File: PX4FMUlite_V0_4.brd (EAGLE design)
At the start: 48.6 x 34.9 mm, 126 parts, among them J2 DF13-4P-1.25V, J201 DF13C-6P-1.25V, J202 DF13C-6P-1.25V, J203 DF13C-6P-1.25V, J3 DF13C-4P-1.25V, J302 DF13C-4P-1.25V, J401 DF13C-4P-1.25V, J403 DF13C-7P-1.25V, J405 DF13C-4P-1.25V, J802 DF13C-3P-1.25V, M3_MOUNT1101 MOUNT-HOLE3.1MM, M3_MOUNT1102 MOUNT-HOLE3.1MM, M3_MOUNT1103 MOUNT-HOLE3.1MM, M3_MOUNT1104 MOUNT-HOLE3.1MM, U101 STM32F4X7VX, U2 MAX3051, U401 MAX3051, X101 3.2x2.5 mm / 24 MHz / 15 ppm

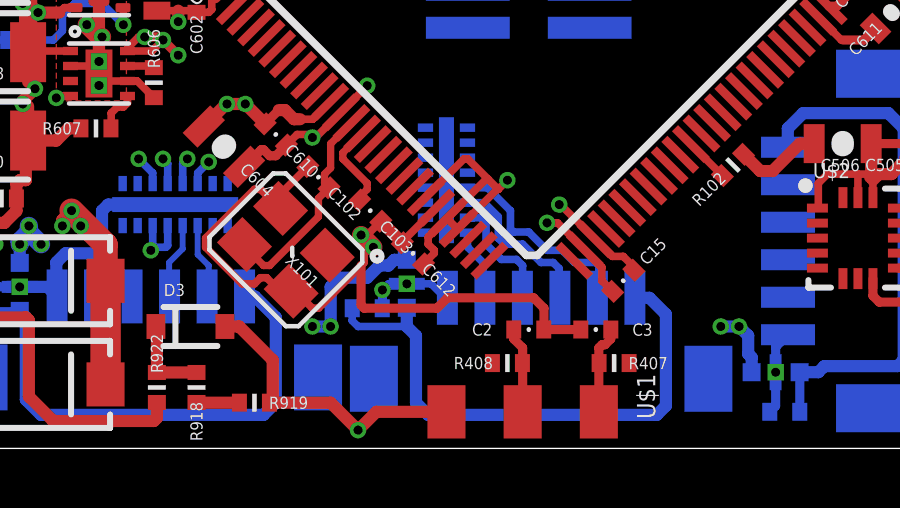
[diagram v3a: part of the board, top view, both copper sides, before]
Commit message: Tweaked power fills to prevent them being isolated after autoroute
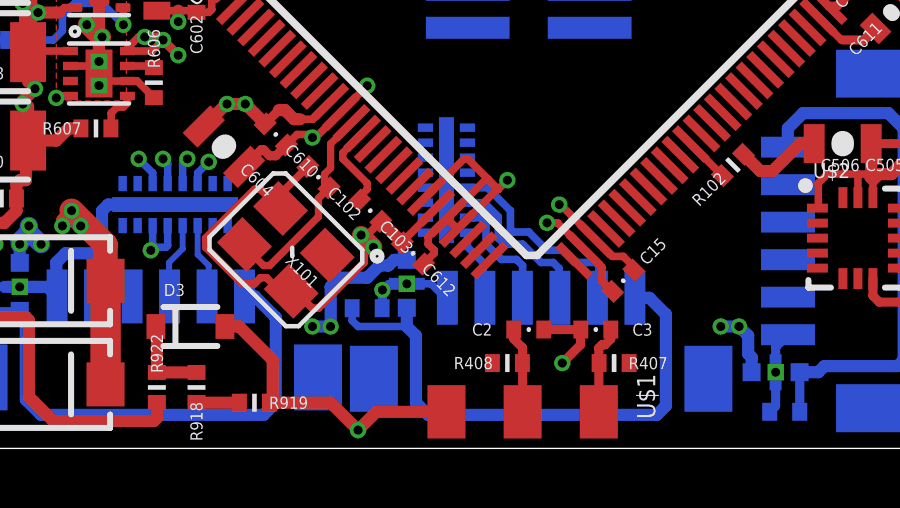
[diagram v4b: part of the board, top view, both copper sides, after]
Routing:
- net GND: track 206.8 -> 199.7 mm, vias 39 -> 40
- net VDD_IN: track 71.6 -> 70.6 mm
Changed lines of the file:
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@@
 <layer number="1" name="Top" color="4" fill="1" visible="yes" active="yes"/>
 <layer number="2" name="Ground" color="2" fill="10" visible="no" active="yes"/>
-<layer number="3" name="Horizontal" color="13" fill="15" visible="no" active="yes"/>
+<layer number="3" name="Horizontal" color="13" fill="15" visible="yes" active="yes"/>
 <layer number="4" name="Route4" color="1" fill="4" visible="no" active="no"/>
 <layer number="5" name="Route5" color="4" fill="4" visible="no" active="no"/>
@@
 <layer number="12" name="Route12" color="1" fill="5" visible="no" active="no"/>
 <layer number="13" name="Route13" color="4" fill="5" visible="no" active="no"/>
-<layer number="14" name="Vertical" color="14" fill="15" visible="no" active="yes"/>
-<layer number="15" name="Power" color="11" fill="15" visible="no" active="yes"/>
+<layer number="14" name="Vertical" color="14" fill="15" visible="yes" active="yes"/>
+<layer number="15" name="Power" color="11" fill="15" visible="yes" active="yes"/>
 <layer number="16" name="Bottom" color="1" fill="1" visible="yes" active="yes"/>
 <layer number="17" name="Pads" color="2" fill="1" visible="yes" active="yes"/>
@@
 <contactref element="U101" pad="6"/>
 <contactref element="R608" pad="P$1"/>
-<wire x1="30.273071875" y1="15.71561875" x2="27.2288" y2="18.1944" width="0" layer="19" extent="1-16"/>
+<wire x1="27.2288" y1="18.1944" x2="30.273071875" y2="15.71561875" width="0" layer="19" extent="1-16"/>
 </signal>
 <signal name="N$11">
@@
 <wire x1="22.7584" y1="10.16" x2="23.368" y2="10.16" width="0.8128" layer="15"/>
 <wire x1="46.6344" y1="30.6832" x2="45.4152" y2="30.6832" width="0.6096" layer="15"/>
-<wire x1="32.4104" y1="29.8704" x2="30.8864" y2="28.3464" width="1.016" layer="15"/>
-<wire x1="30.8864" y1="28.3464" x2="28.6512" y2="28.3464" width="1.016" layer="15"/>
-<wire x1="28.6512" y1="28.3464" x2="27.3304" y2="27.0256" width="1.016" layer="15"/>
+<wire x1="34.1376" y1="33.8328" x2="27.3304" y2="27.0256" width="1.016" layer="15"/>
 <wire x1="27.3304" y1="27.0256" x2="25.6032" y2="27.0256" width="1.016" layer="15"/>
 <wire x1="25.6032" y1="27.0256" x2="24.2824" y2="25.7048" width="1.016" layer="15"/>
 <wire x1="24.2824" y1="25.7048" x2="24.2824" y2="24.892" width="1.016" layer="15"/>
-<wire x1="32.4104" y1="29.8704" x2="33.528" y2="30.988" width="0.8128" layer="15"/>
-<wire x1="33.528" y1="30.988" x2="33.528" y2="32.7152" width="0.8128" layer="15"/>
-<wire x1="33.528" y1="32.7152" x2="34.6456" y2="33.8328" width="0.8128" layer="15"/>
-<wire x1="40.132" y1="33.8328" x2="34.6456" y2="33.8328" width="0.8128" layer="15"/>
+<wire x1="40.132" y1="33.8328" x2="34.1376" y2="33.8328" width="0.8128" layer="15"/>
 <wire x1="40.132" y1="33.8328" x2="40.132" y2="33.7312" width="0.8128" layer="15"/>
 <wire x1="40.132" y1="33.7312" x2="42.164" y2="31.6992" width="0.8128" layer="15"/>
@@
 <wire x1="33.373553125" y1="10.31444375" x2="32.8168" y2="9.757690625" width="0.254" layer="1"/>
 <wire x1="32.8168" y1="9.757690625" x2="32.8168" y2="8.9408" width="0.254" layer="1"/>
-<wire x1="32.8168" y1="8.9408" x2="32.7152" y2="8.8392" width="0.254" layer="1"/>
-<wire x1="32.7152" y1="8.8392" x2="31.2928" y2="7.4168" width="0.254" layer="1"/>
+<wire x1="32.8168" y1="8.9408" x2="31.2928" y2="7.4168" width="0.254" layer="1"/>
 <wire x1="31.2928" y1="7.4168" x2="31.0896" y2="7.4168" width="0.254" layer="1"/>
 <wire x1="31.0896" y1="7.4168" x2="30.522059375" y2="7.984340625" width="0.254" layer="1"/>
@@
 <wire x1="41.09515625" y1="7.97764375" x2="41.09924375" y2="7.97764375" width="0.254" layer="1"/>
 <wire x1="38.8032" y1="6.7056" x2="38.8112" y2="6.7136" width="0.3048" layer="1"/>
-<wire x1="38.8112" y1="6.7136" x2="38.8112" y2="7.4168" width="0.3048" layer="1"/>
-<wire x1="38.8112" y1="7.4168" x2="38.464" y2="7.764" width="0.3048" layer="1"/>
-<wire x1="38.464" y1="7.764" x2="35.591" y2="7.764" width="0.3048" layer="1"/>
-<wire x1="35.591" y1="7.764" x2="35.2438" y2="7.4168" width="0.3048" layer="1"/>
-<wire x1="35.2438" y1="7.4168" x2="32.8168" y2="7.4168" width="0.3048" layer="1"/>
-<wire x1="32.8168" y1="7.4168" x2="32.7152" y2="7.5184" width="0.3048" layer="1"/>
-<wire x1="32.7152" y1="7.5184" x2="32.7152" y2="8.8392" width="0.3048" layer="1"/>
 <wire x1="40.71926875" y1="31.315128125" x2="40.71926875" y2="31.37206875" width="0.4064" layer="1"/>
 <wire x1="40.71926875" y1="31.37206875" x2="41.148" y2="31.8008" width="0.4064" layer="1"/>
@@
 <wire x1="20.9376" y1="16.3576" x2="20.2184" y2="16.3576" width="0.254" layer="16"/>
 <wire x1="20.2184" y1="16.3576" x2="18.8976" y2="17.6784" width="0.254" layer="16"/>
+<wire x1="40.0384" y1="6.7056" x2="40.0304" y2="6.6976" width="0.3048" layer="1"/>
+<wire x1="40.0304" y1="6.6976" x2="40.0304" y2="6.1976" width="0.3048" layer="1"/>
+<wire x1="40.0304" y1="6.1976" x2="39.4208" y2="5.588" width="0.3048" layer="1"/>
+<via x="39.4208" y="5.588" extent="1-16" drill="0.3"/>
 <wire x1="52.324" y1="23.6728" x2="52.324" y2="24.0728" width="0" layer="19" extent="16-16"/>
 <wire x1="29.51684375" y1="13.56564375" x2="29.51684375" y2="13.561553125" width="0" layer="19" extent="1-1"/>
 <wire x1="52.324" y1="23.2728" x2="52.324" y2="23.368" width="0" layer="19" extent="1-16"/>
 <wire x1="32.8168" y1="9.757690625" x2="32.7152" y2="9.8552" width="0" layer="19" extent="1-1"/>
-<wire x1="35.591" y1="7.764" x2="35.591" y2="7.764" width="0" layer="19" extent="1-16"/>
 <wire x1="46.228" y1="26.7272" x2="46.228" y2="26.416" width="0" layer="19" extent="16-16"/>
 <wire x1="42.4688" y1="32.2136" x2="42.4688" y2="31.9024" width="0" layer="19" extent="1-16"/>
@@
 <wire x1="46.5328" y1="5.6832" x2="46.5328" y2="5.2832" width="0" layer="19" extent="16-16"/>
 <wire x1="46.5328" y1="4.8832" x2="46.5328" y2="5.2832" width="0" layer="19" extent="16-16"/>
+<wire x1="34.6392" y1="8.2296" x2="34.2392" y2="8.2296" width="0" layer="19" extent="16-16"/>
 <wire x1="21.736" y1="8.128" x2="21.336" y2="8.128" width="0" layer="19" extent="16-16"/>
 <wire x1="22.253" y1="22.768" x2="21.328" y2="22.868" width="0" layer="19" extent="1-1"/>
@@
 <vertex x="35.2552" y="33.02"/>
 <vertex x="34.3408" y="32.1056"/>
-<vertex x="34.3408" y="30.6832"/>
-<vertex x="30.7848" y="27.1272"/>
-<vertex x="28.8544" y="27.1272"/>
+<vertex x="33.8328" y="32.1056"/>
 <vertex x="25.1968" y="23.4696"/>
 <vertex x="25.1968" y="19.2024"/>

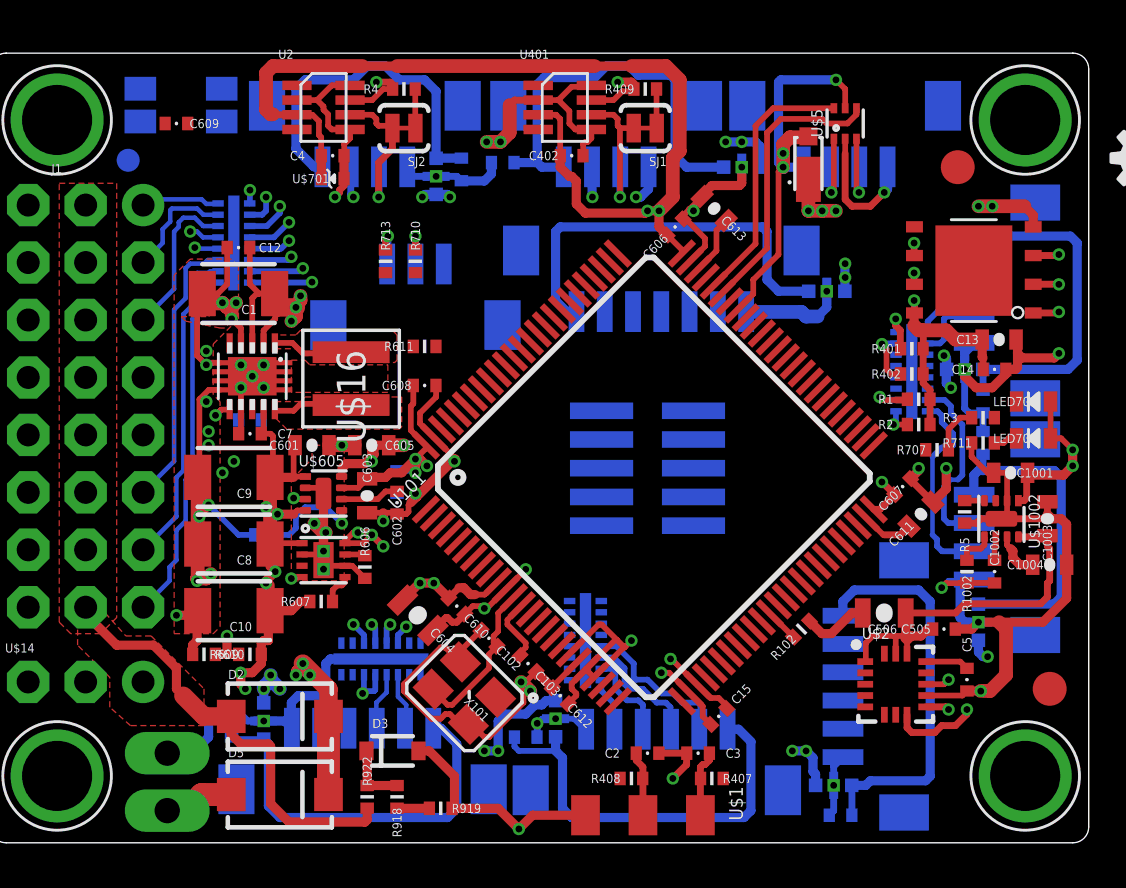
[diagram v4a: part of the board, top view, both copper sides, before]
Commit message: Routed safety switch resistor
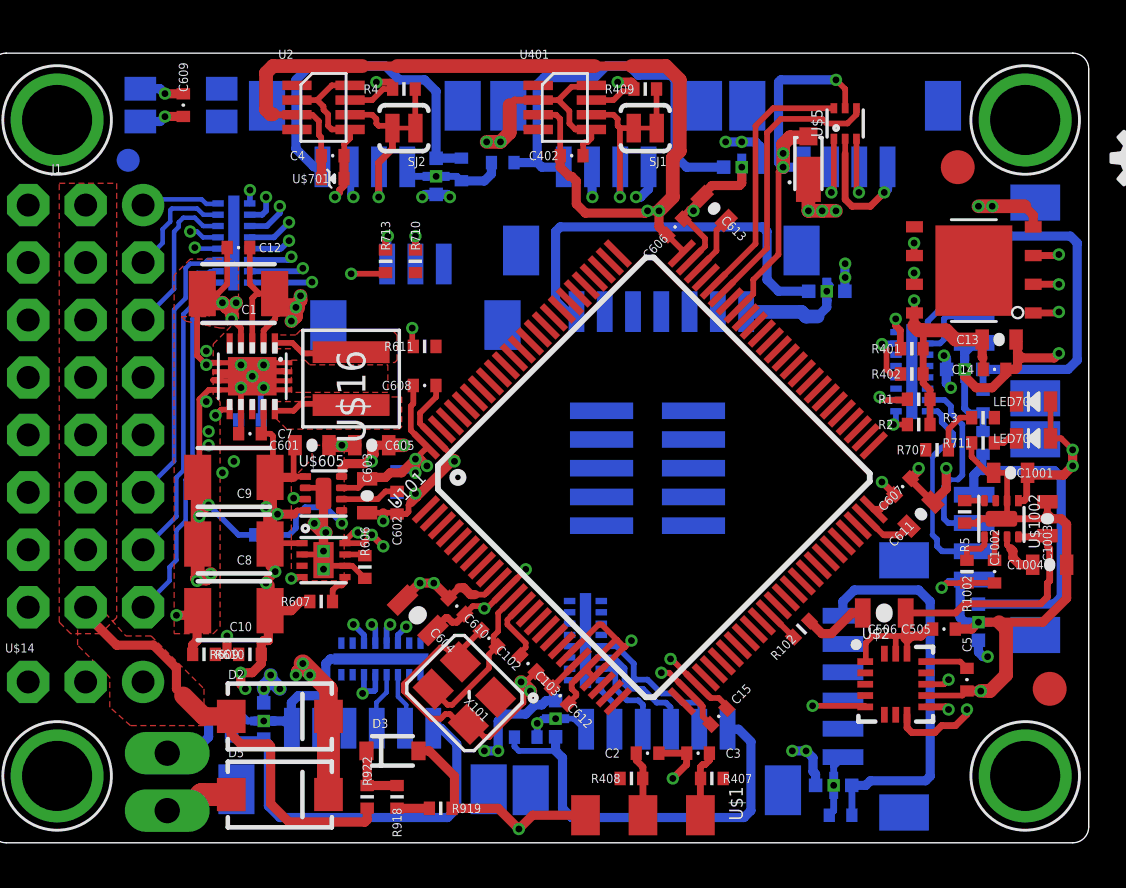
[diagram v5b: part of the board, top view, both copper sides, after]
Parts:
- moved C609 0.87 mm to (17.8, 35.4), turned to 270 degrees
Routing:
- net GND: track 199.7 -> 213.8 mm, vias 40 -> 44
- net FMU-!RESET: track 0.54 -> 2.53 mm, vias 1 -> 2
- net VDD_5V: track 84.9 -> 85.5 mm

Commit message: Tweak
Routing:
- net FMU_AUX_ADC1: track 0.00 -> 0.72 mm, vias 0 -> 1
- net FMU_AUX_ADC2: track 0.00 -> 0.52 mm, vias 0 -> 1
